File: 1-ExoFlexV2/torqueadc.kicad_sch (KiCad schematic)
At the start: 42 parts, among them J86 Jumper, J87 Jumper, J88 Jumper, U33 OP-AMP, U34 OP-AMP, U35 OP-AMP, U36 OP-AMP, U37 OP-AMP, U38 OP-AMP, U39 OP-AMP, U40 OP-AMP, U41 OP-AMP

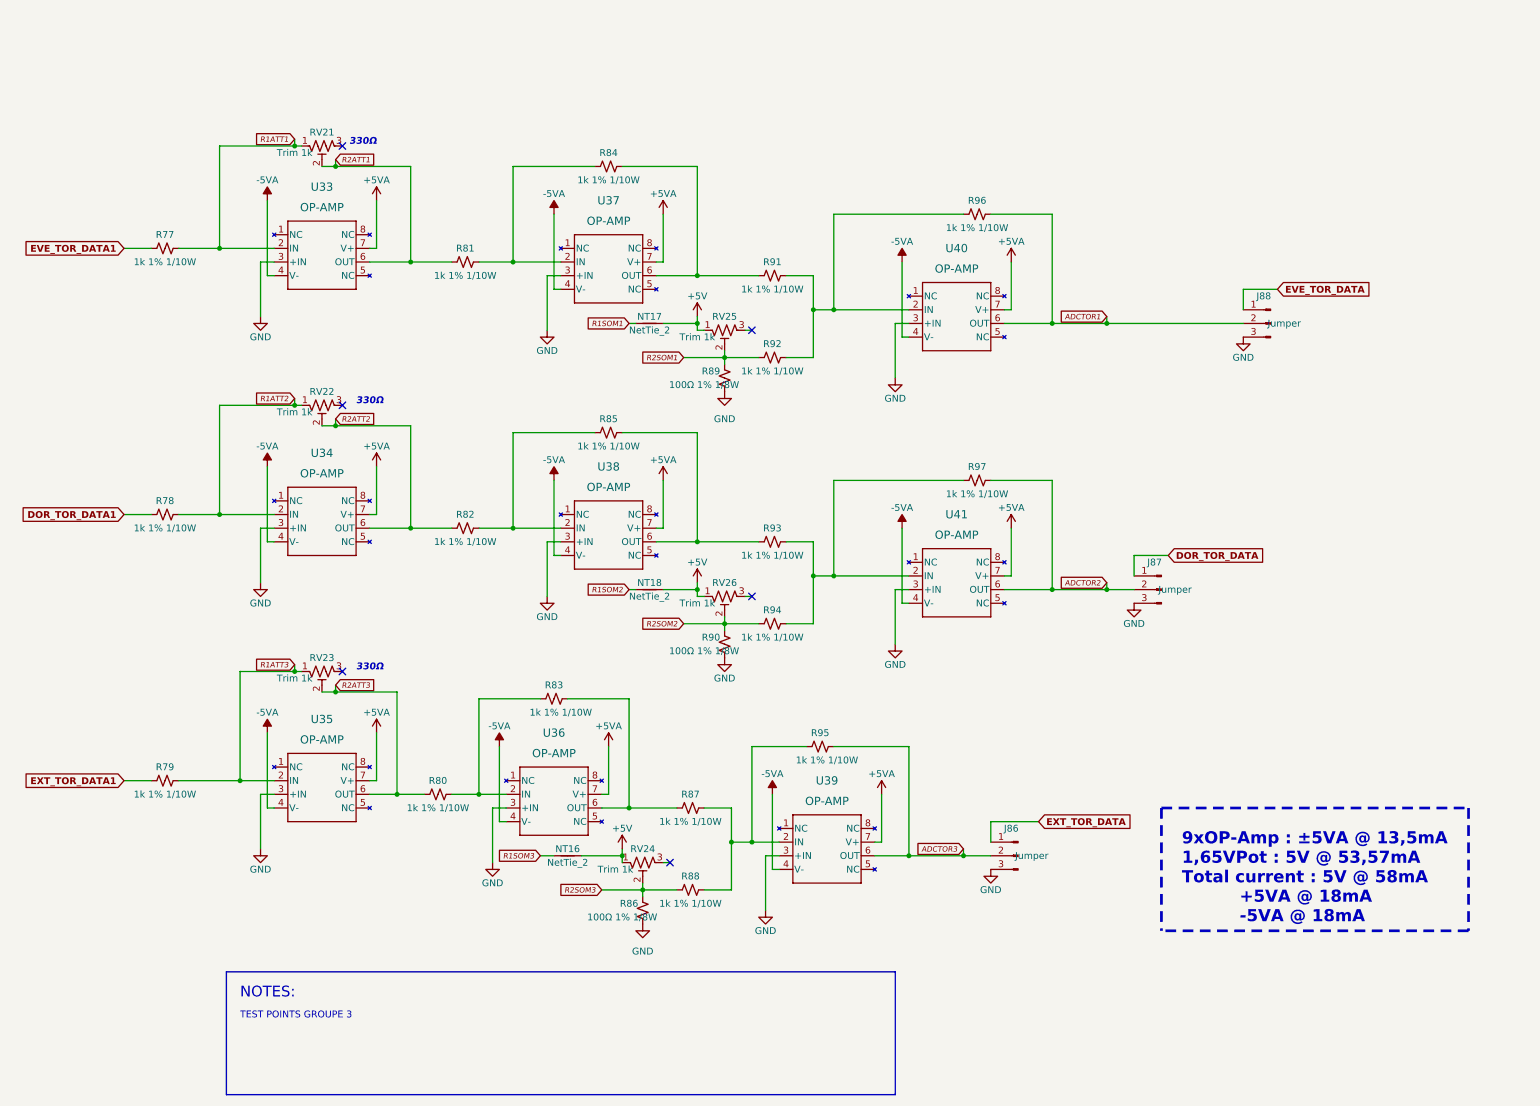
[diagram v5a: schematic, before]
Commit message: Finalisation 3
- Changement des régulateur de tension
- Retrait de test point inutile
- Changement de jumper mal positionner
- Ajout de Mounting holes et fiducial
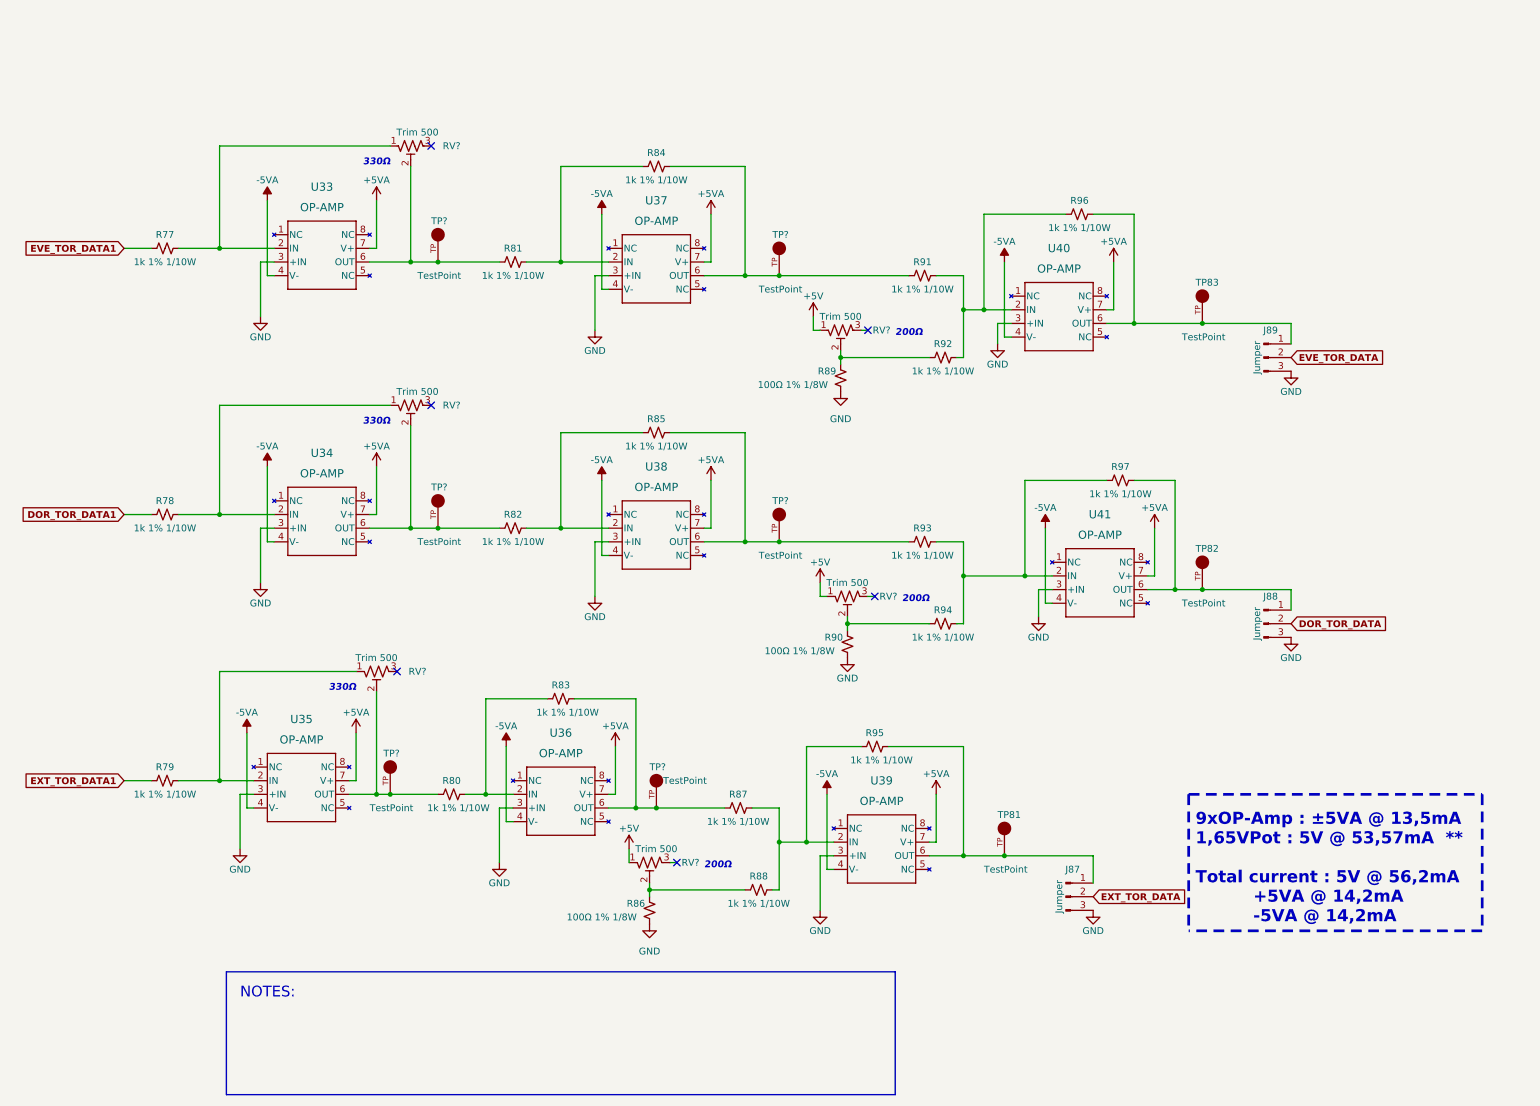
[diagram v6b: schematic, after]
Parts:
- removed NT16, NT17, NT18: NetTie_2, NetTie:NetTie-2_SMD_Pad0.5mm, symbol Device:NetTie_2
- removed RV21, RV22, RV23, RV24, RV25, RV26: Trim 1k, FootPrint:TRIM_3362P-1-102LF, symbol Device:R_Potentiometer_Trim_US
- added RV? (x6): Trim 500, FootPrint:TRIM_3296W-1-501LF, symbol Device:R_Potentiometer_Trim_US
- added TP81, TP82, TP83, TP? (x6): TestPoint, FootPrint:KEYSTONE_5005, symbol SymLib:5005
- J87: renamed from J86; footprint Connector_PinSocket_2.54mm:PinSocket_1x03_P2.54mm_Vertical -> Connector_PinHeader_2.54mm:PinHeader_1x03_P2.54mm_Vertical
- J88: renamed from J87; footprint Connector_PinSocket_2.54mm:PinSocket_1x03_P2.54mm_Vertical -> Connector_PinHeader_2.54mm:PinHeader_1x03_P2.54mm_Vertical
- J89: renamed from J88; footprint Connector_PinSocket_2.54mm:PinSocket_1x03_P2.54mm_Vertical -> Connector_PinHeader_2.54mm:PinHeader_1x03_P2.54mm_Vertical
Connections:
- net +5V: now also RV?.1, RV?.1, RV?.1
- net DOR_TOR_DATA: now also J88.2 (Pin_2); no longer J88.1 (Pin_1)
- net EVE_TOR_DATA: now also J89.2 (Pin_2); no longer J89.1 (Pin_1)
- net EXT_TOR_DATA: now also J87.2 (Pin_2); no longer J87.1 (Pin_1)
- net at R84.2, R91.1, U37.6 (OUT): now also TP?.TP
- net at R83.2, R87.1, U36.6 (OUT): now also TP?.TP
- net at R85.2, R93.1, U38.6 (OUT): now also TP?.TP
- net ADCTOR1: no longer names the net of R96.2, U40.6 (OUT)
- net ADCTOR1: now also J89.1 (Pin_1), TP83.TP; no longer J89.2 (Pin_2)
- net ADCTOR2: no longer names the net of R97.2, U41.6 (OUT)
- net ADCTOR2: now also J88.1 (Pin_1), TP82.TP; no longer J88.2 (Pin_2)
- net ADCTOR3: no longer names the net of R95.2, U39.6 (OUT)
- net ADCTOR3: now also J87.1 (Pin_1), TP81.TP; no longer J87.2 (Pin_2)
- net R1ATT1: no longer names the net of R77.2, U33.2 (IN)
- net R1ATT1: now also RV?.1
- net R1ATT2: no longer names the net of R78.2, U34.2 (IN)
- net R1ATT2: now also RV?.1
- net R1ATT3: no longer names the net of R79.2, U35.2 (IN)
- net R1ATT3: now also RV?.1
- net R2ATT1: no longer names the net of R81.1, U33.6 (OUT)
- net R2ATT1: now also RV?.2, TP?.TP
- net R2ATT2: no longer names the net of R82.1, U34.6 (OUT)
- net R2ATT2: now also RV?.2, TP?.TP
- net R2ATT3: no longer names the net of R80.1, U35.6 (OUT)
- net R2ATT3: now also RV?.2, TP?.TP
- net R2SOM1: no longer names the net of R89.2, R92.1
- net R2SOM1: now also RV?.2
- net R2SOM2: no longer names the net of R90.2, R94.1
- net R2SOM2: now also RV?.2
- net R2SOM3: no longer names the net of R86.2, R88.1
- net R2SOM3: now also RV?.2
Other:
- note added: "200Ω"
- note added: "9xOP-Amp : ±5VA @ 13,5mA 1,65VPot : 5V @ 53,57mA ** Total current : 5V @ 56,2mA +5VA @ 14,2mA -5VA @ 14,2mA"
- note removed: "9xOP-Amp : ±5VA @ 13,5mA 1,65VPot : 5V @ 53,57mA Total current : 5V @ 58mA +5VA @ 18mA -5VA @ 18mA"
- note removed: "TEST POINTS GROUPE 3"
- moved on the sheet: J87, J88, J89, R80, R81, R82, R83, R84, R85, R86, R87, R88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

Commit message: Finalisation schéma FIN
- Changement des uméro pour les inverseurs
- Changement des connecteur et début de placement
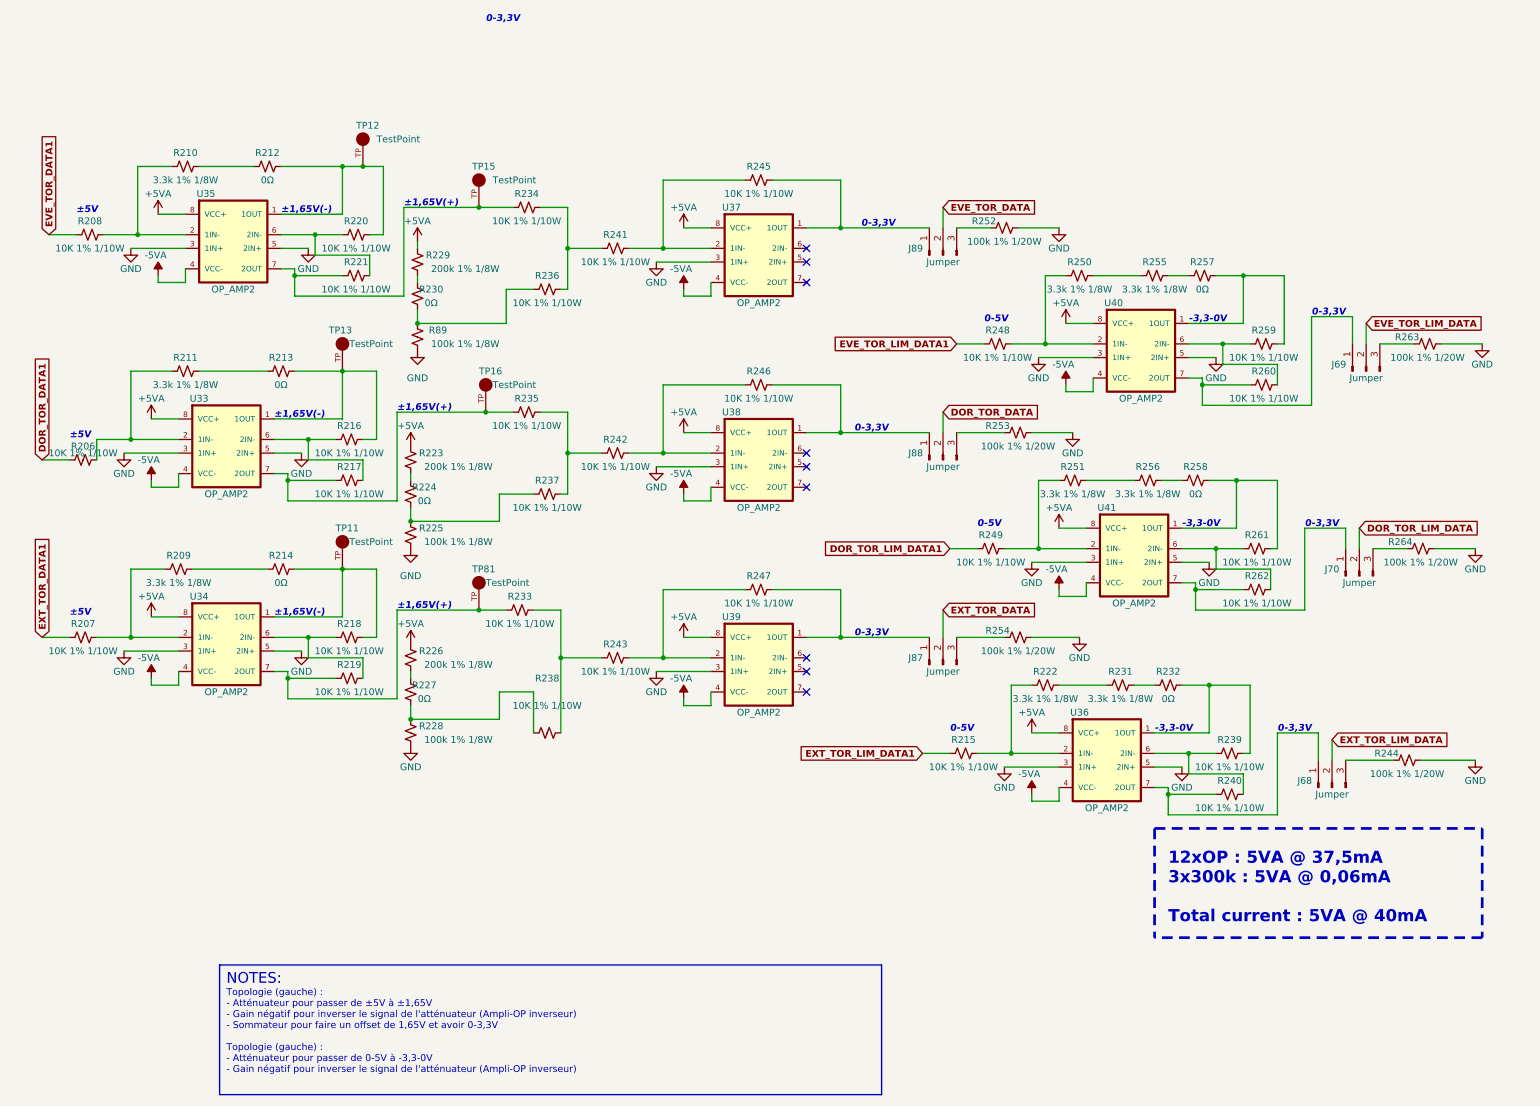
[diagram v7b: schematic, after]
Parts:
- removed R77, R78, R79, R80, R81, R82, R83, R84, R85, R87, R88, R91, R92, R93, R94, R95, R96, R97: 1k 1% 1/10W, Resistor_SMD:R_0805_2012Metric, symbol Device:R_Small_US
- removed R86, R90: 100Ω 1% 1/8W, Resistor_SMD:R_0805_2012Metric, symbol Device:R_Small_US
- removed RV? (x6): Trim 500, FootPrint:TRIM_3296W-1-501LF, symbol Device:R_Potentiometer_Trim_US
- removed TP82, TP83, TP?: TestPoint, FootPrint:KEYSTONE_5005, symbol SymLib:5005
- removed U33, U34, U35, U36, U37, U38, U39, U40, U41: OP-AMP, DGK8_TEX, symbol SymLib:OPA197IDGKR
- added J68, J69, J70: Jumper, Connector_PinHeader_2.54mm:PinHeader_1x03_P2.54mm_Vertical, symbol Connector:Conn_01x03_Male
- added R206, R207, R208, R215, R216, R217, R218, R219, R220, R221, R233, R234, R235, R236, R237, R238, R239, R240, R241, R242, R243, R245, R246, R247, R248, R249, R259, R260, R261, R262: 10K 1% 1/10W, Resistor_SMD:R_0603_1608Metric, symbol Device:R_Small_US
- added R209, R210, R211, R222, R231, R250, R251, R255, R256: 3.3k 1% 1/8W, Resistor_SMD:R_0805_2012Metric, symbol Device:R_Small_US
- added R212, R213, R214, R224, R227, R230, R232, R257, R258: 0Ω, Resistor_SMD:R_0805_2012Metric, symbol Device:R_Small_US
- added R223, R226, R229: 200k 1% 1/8W, Resistor_SMD:R_0805_2012Metric, symbol Device:R_Small_US
- added R225, R228: 100k 1% 1/8W, Resistor_SMD:R_0805_2012Metric, symbol Device:R_Small_US
- added R244, R252, R253, R254, R263, R264: 100k 1% 1/20W, Resistor_SMD:R_0201_0603Metric, symbol Device:R_Small_US
- added U33, U34, U35, U36, U37, U38, U39, U40, U41: OP_AMP2, FootPrintLib:SOIC127P599X175-8N, symbol SymLib:TL072IDR
- R89: value 100Ω 1% 1/8W -> 100k 1% 1/8W; DESCRIPTION 100 Ohms ±1% 0.125W, 1/8W Chip Resistor 0805 (2012 Metric) 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 -> 100 kOhms ±1% 0.125W, 1/8W Chip Resistor 0805 (2012 Metric)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; PART NUMBER ERJ-6ENF1000V -> ERJ-6ENF1003V
- TP11, TP12, TP13, TP15, TP16: renamed from TP?; NOTES (none) -> DO NOT POPULATE; PURCHASE-URL https://pricing.snapeda.com/search/part/5005/?ref=eda -> (none)
- TP81: NOTES (none) -> DO NOT POPULATE; PURCHASE-URL https://pricing.snapeda.com/search/part/5005/?ref=eda -> (none)
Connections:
- net +5VA: now also R223.2, R226.2, R229.2, U33.8 (VCC+), U34.8 (VCC+), U35.8 (VCC+), U36.8 (VCC+), U37.8 (VCC+), U38.8 (VCC+), U39.8 (VCC+), U40.8 (VCC+), U41.8 (VCC+)
- net -5VA: now also U33.4 (VCC-), U34.4 (VCC-), U35.4 (VCC-), U36.4 (VCC-), U37.4 (VCC-), U38.4 (VCC-), U39.4 (VCC-), U40.4 (VCC-), U41.4 (VCC-)
- net DOR_TOR_DATA1: now also R206.1
- net EVE_TOR_DATA1: now also R208.1
- net EXT_TOR_DATA1: now also R207.1
- net GND: now also R225.1, R228.1, R244.2, R252.2, R253.2, R254.2, R263.2, R264.2, U33.3 (1IN+), U33.5 (2IN+), U34.3 (1IN+), U34.5 (2IN+), U35.3 (1IN+), U35.5 (2IN+), U36.3 (1IN+), U36.5 (2IN+), U37.3 (1IN+), U38.3 (1IN+), U39.3 (1IN+), U40.3 (1IN+), U40.5 (2IN+), U41.3 (1IN+), U41.5 (2IN+); no longer J87.3 (Pin_3), J88.3 (Pin_3), J89.3 (Pin_3)
- net at TP81.TP: now also R219.1, R233.1, U34.7 (2OUT); no longer J87.1 (Pin_1)
- net at TP15.TP: now also R221.1, R234.1, U35.7 (2OUT)
- net at TP11.TP: now also R214.2, R218.2, U34.1 (1OUT)
- net at TP12.TP: now also R212.2, R220.2, U35.1 (1OUT)
- net at TP16.TP: now also R217.1, R235.1, U33.7 (2OUT)
- net at J89.1 (Pin_1): now also R245.2, U37.1 (1OUT)
- net at TP13.TP: now also R213.2, R216.2, U33.1 (1OUT)
- net at R89.2: now also R230.1, R236.1
- net at J88.1 (Pin_1): now also R246.2, U38.1 (1OUT)
- new net: R218.1, R219.2, U34.6 (2IN-)
- new net: R207.2, R209.1, U34.2 (1IN-)
- new net: R209.2, R214.1
- new net: R234.2, R236.2, R241.1
- new net: R206.2, R211.1, U33.2 (1IN-)
- new net: R223.1, R224.2
- new net: R216.1, R217.2, U33.6 (2IN-)
- new net: J69.3 (Pin_3), R263.1
- new net: R249.2, R251.1, U41.2 (1IN-)
- new net: R251.2, R256.1
- new net: R248.2, R250.1, U40.2 (1IN-)
- new net: R227.1, R228.2, R238.1
- new net: R226.1, R227.2
- new net: R250.2, R255.1
- new net: R255.2, R257.1
- new net: R224.1, R225.2, R237.1
- new net: R235.2, R237.2, R242.1
- new net: J68.1 (Pin_1), R240.1, U36.7 (2OUT)
- new net: J68.3 (Pin_3), R244.1
- new net: R256.2, R258.1
- new net: R258.2, R261.2, U41.1 (1OUT)
- new net: R233.2, R238.2, R243.1
- new net: R220.1, R221.2, U35.6 (2IN-)
- new net: R242.2, R246.1, U38.2 (1IN-)
- new net: R229.1, R230.2
- new net: R208.2, R210.1, U35.2 (1IN-)
- new net: R210.2, R212.1
- new net: R243.2, R247.1, U39.2 (1IN-)
- new net: J87.1 (Pin_1), R247.2, U39.1 (1OUT)
- new net: J69.1 (Pin_1), R260.1, U40.7 (2OUT)
- new net: J87.3 (Pin_3), R254.1
- new net: R241.2, R245.1, U37.2 (1IN-)
- new net: R231.2, R232.1
- new net: R232.2, R239.2, U36.1 (1OUT)
- new net: R215.2, R222.1, U36.2 (1IN-)
- new net: R211.2, R213.1
- new net: R239.1, R240.2, U36.6 (2IN-)
- new net: R259.1, R260.2, U40.6 (2IN-)
- new net: R257.2, R259.2, U40.1 (1OUT)
- new net: J70.3 (Pin_3), R264.1
- new net: J89.3 (Pin_3), R252.1
- new net: R261.1, R262.2, U41.6 (2IN-)
- new net: J88.3 (Pin_3), R253.1
- new net: J70.1 (Pin_1), R262.1, U41.7 (2OUT)
- new net: R222.2, R231.1
- new net DOR_TOR_LIM_DATA: J70.2 (Pin_2)
- new net DOR_TOR_LIM_DATA1: R249.1
- new net EVE_TOR_LIM_DATA: J69.2 (Pin_2)
- new net EVE_TOR_LIM_DATA1: R248.1
- new net EXT_TOR_LIM_DATA: J68.2 (Pin_2)
- new net EXT_TOR_LIM_DATA1: R215.1
- no-connect marks 6 -> 9
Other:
- note added: "-3,3-0V"
- note added: "0-3,3V"
- note added: "0-5V"
- note added: "12xOP : 5VA @ 37,5mA 3x300k : 5VA @ 0,06mA Total current : 5VA @ 40mA"
- note added: "Topologie (gauche) : - Atténuateur pour passer de ±5V à ±1,65V - Gain négatif pour inverser le signal de l'atténuateur (Ampli-OP inverseur) - Sommateur pour faire un offset de 1,65V et avoir 0-3,3V Topologie (gauche) : - Atténuateur pour passer de 0-5V à -3,3-0V - Gain négatif pour inverser le signal de l'atténuateur (Ampli-OP inverseur)"
- note added: "±1,65V(+)"
- note added: "±1,65V(-)"
- note added: "±5V"
- note removed: "200Ω"
- note removed: "330Ω"
- note removed: "9xOP-Amp : ±5VA @ 13,5mA 1,65VPot : 5V @ 53,57mA ** Total current : 5V @ 56,2mA +5VA @ 14,2mA -5VA @ 14,2mA"
- moved on the sheet: J87, J88, J89, R89, TP11, TP12, TP13, TP15, TP16, TP81
